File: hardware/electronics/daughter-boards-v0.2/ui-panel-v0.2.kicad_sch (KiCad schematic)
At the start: 9 parts

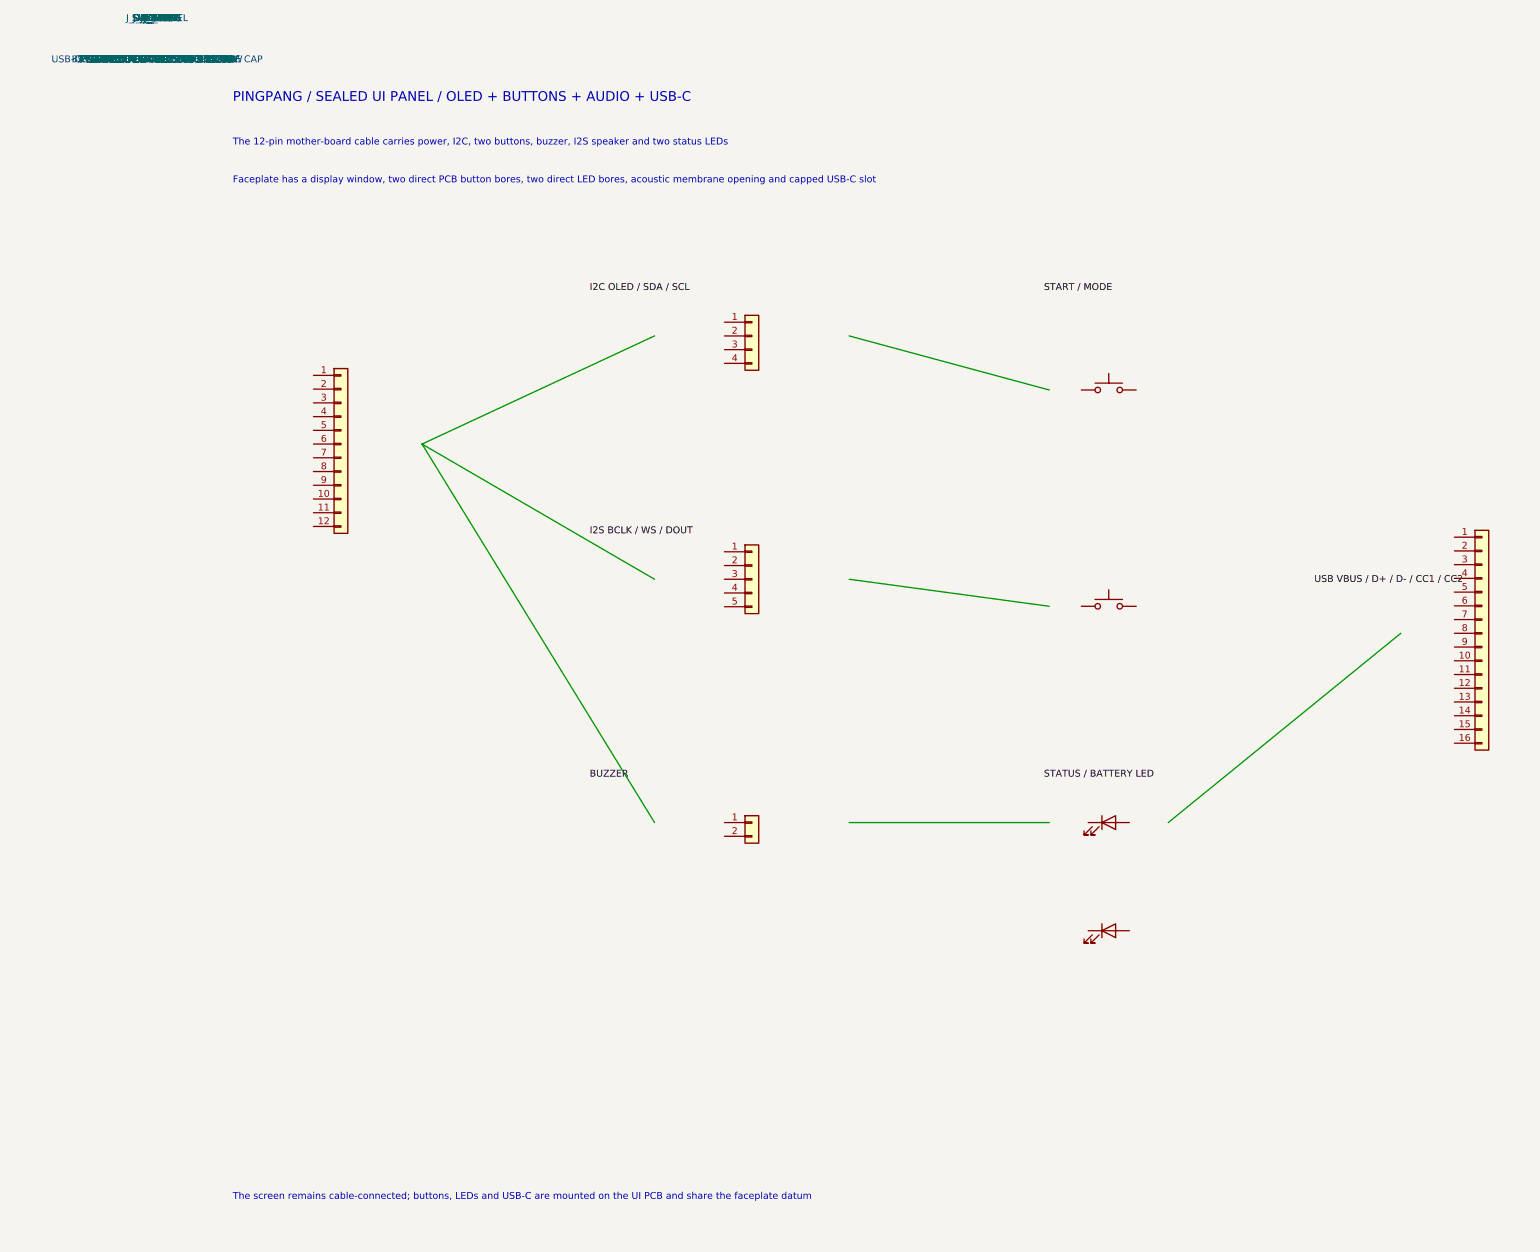
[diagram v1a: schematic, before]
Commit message: 🔌 统一 Type-C 充电入口
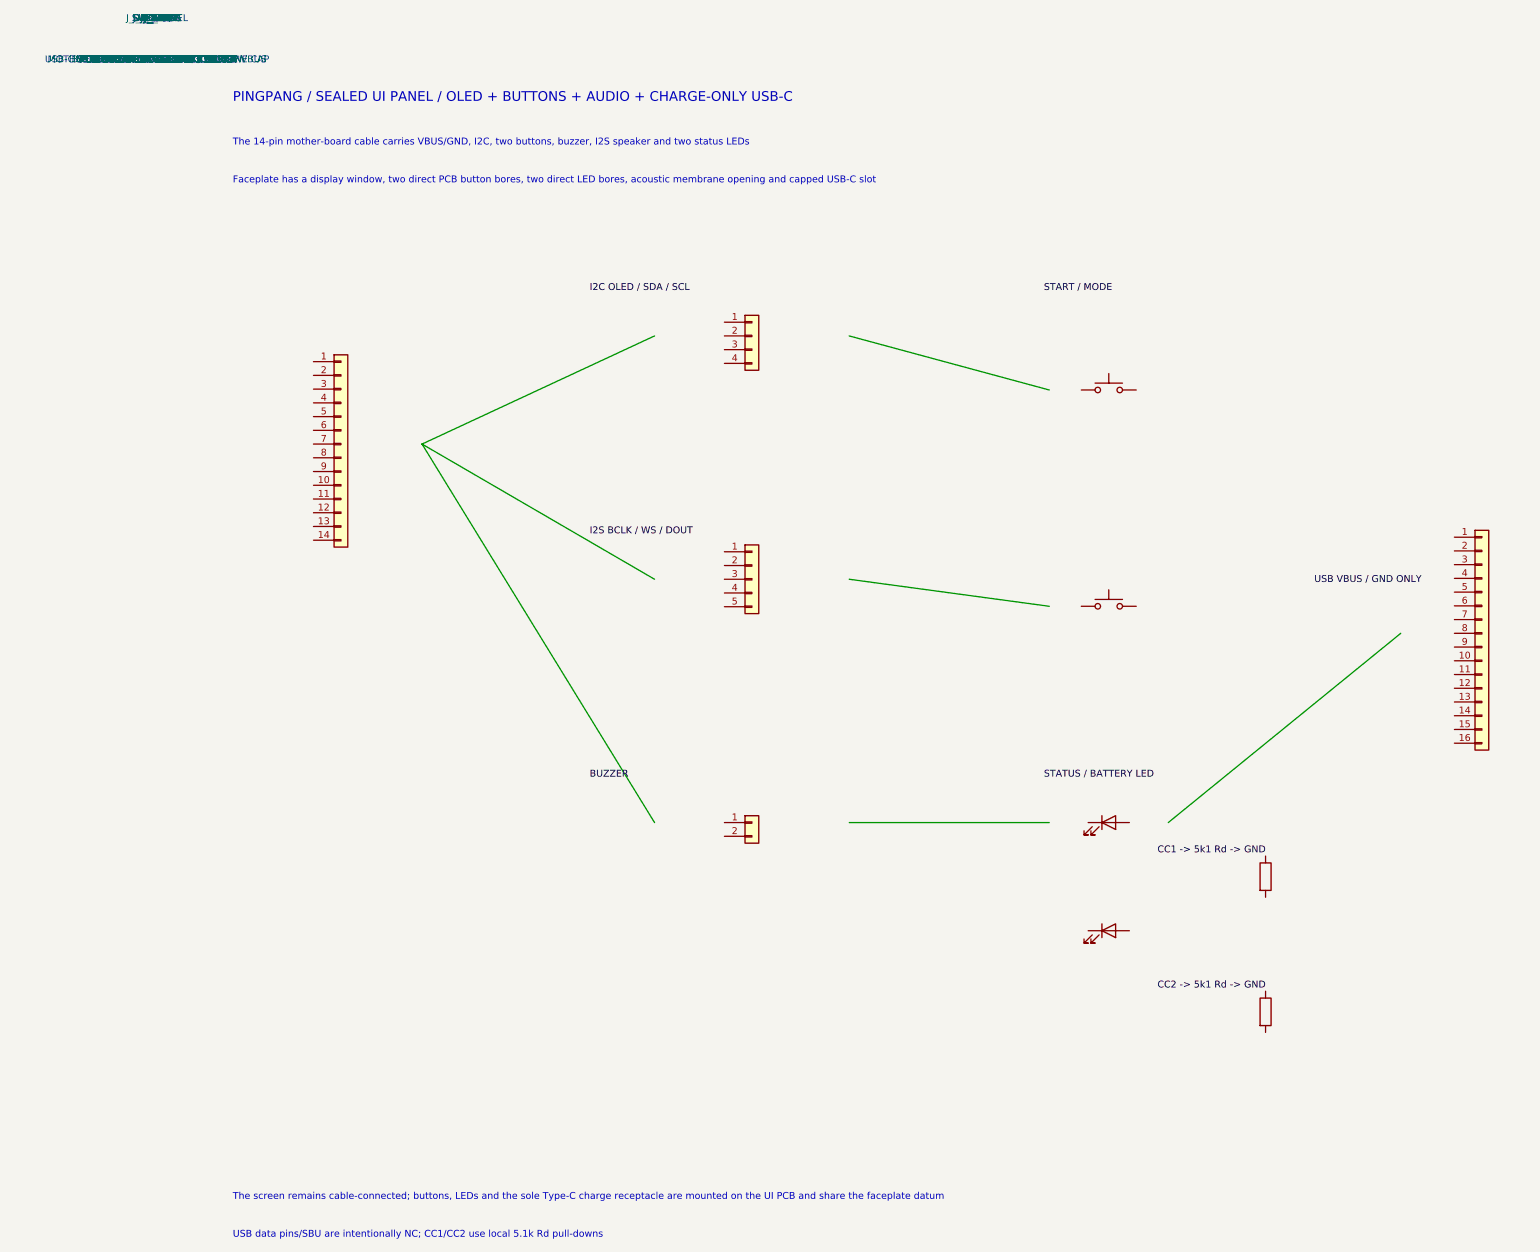
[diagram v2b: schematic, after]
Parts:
- removed J_MOTHER: MOTHER UI MX1.25 LOCK 12P, Connector_JST:JST_GH_SM12B-GHS-TB_1x12-1MP_P1.25mm_Horizontal, symbol Connector_Generic:Conn_01x12
- added J_MOTHER: MOTHER UI MX1.25 LOCK 14P / CHARGE VBUS, Connector_JST:JST_GH_SM14B-GHS-TB_1x14-1MP_P1.25mm_Horizontal, symbol Connector_Generic:Conn_01x14
- added R_CC1: USB-C CC1 Rd 5k1, Resistor_SMD:R_0603_1608Metric, symbol Device:R
- added R_CC2: USB-C CC2 Rd 5k1, Resistor_SMD:R_0603_1608Metric, symbol Device:R
- J_USB_PANEL: value USB-C VERTICAL 16P DIRECT / SILICONE CAP -> USB-C VERTICAL CHARGE-ONLY / SILICONE CAP
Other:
- note added: "PINGPANG / SEALED UI PANEL / OLED + BUTTONS + AUDIO + CHARGE-ONLY USB-C"
- note added: "The 14-pin mother-board cable carries VBUS/GND, I2C, two buttons, buzzer, I2S speaker and two status LEDs"
- note added: "The screen remains cable-connected; buttons, LEDs and the sole Type-C charge receptacle are mounted on the UI PCB and share the faceplate datum"
- note added: "USB data pins/SBU are intentionally NC; CC1/CC2 use local 5.1k Rd pull-downs"
- note removed: "PINGPANG / SEALED UI PANEL / OLED + BUTTONS + AUDIO + USB-C"
- note removed: "The 12-pin mother-board cable carries power, I2C, two buttons, buzzer, I2S speaker and two status LEDs"
- note removed: "The screen remains cable-connected; buttons, LEDs and USB-C are mounted on the UI PCB and share the faceplate datum"
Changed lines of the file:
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@@
 		(comment 3 "Mechanical package is checked separately against net_stand.scad")
 	)
-	(text "PINGPANG / SEALED UI PANEL / OLED + BUTTONS + AUDIO + USB-C"
+	(text "PINGPANG / SEALED UI PANEL / OLED + BUTTONS + AUDIO + CHARGE-ONLY USB-C"
 		(exclude_from_sim no)
 		(at 14 12 0)
 		(effects (font (size 1.8 1.8)) (justify left bottom))
 	)
-	(text "The 12-pin mother-board cable carries power, I2C, two buttons, buzzer, I2S speaker and two status LEDs"
+	(text "The 14-pin mother-board cable carries VBUS/GND, I2C, two buttons, buzzer, I2S speaker and two status LEDs"
 		(exclude_from_sim no)
 		(at 14 20 0)
@@
 		(effects (font (size 1.27 1.27)) (justify left bottom))
 	)
-	(text "The screen remains cable-connected; buttons, LEDs and USB-C are mounted on the UI PCB and share the faceplate datum"
+	(text "The screen remains cable-connected; buttons, LEDs and the sole Type-C charge receptacle are mounted on the UI PCB and share the faceplate datum"
 		(exclude_from_sim no)
 		(at 14 215 0)
+		(effects (font (size 1.27 1.27)) (justify left bottom))
+	)
+	(text "USB data pins/SBU are intentionally NC; CC1/CC2 use local 5.1k Rd pull-downs"
+		(exclude_from_sim no)
+		(at 14 222 0)
 		(effects (font (size 1.27 1.27)) (justify left bottom))
 	)
@@
 		)
 	)
-	(label "USB VBUS / D+ / D- / CC1 / CC2"
+	(label "USB VBUS / GND ONLY"
 		(at 214 101 0)
 		(effects
@@
 		)
 	)
-	(symbol
-		(lib_id "Connector_Generic:Conn_01x12")
+	(label "CC1 -> 5k1 Rd -> GND"
+		(at 185 151 0)
+		(effects
+			(font (size 1.27 1.27))
+			(justify left bottom)
+		)
+	)
+	(label "CC2 -> 5k1 Rd -> GND"
+		(at 185 176 0)
+		(effects
+			(font (size 1.27 1.27))
+			(justify left bottom)
+		)
+	)
+	(symbol
+		(lib_id "Connector_Generic:Conn_01x14")
 		(at 34 75 0)
 		(unit 1)
@@
 			)
 		)
-		(property "Value" "MOTHER UI MX1.25 LOCK 12P"
-			(at 0 3.81 0)
-			(effects
-				(font
-					(size 1.27 1.27)
-				)
-			)
-		)
-		(property "Footprint" "Connector_JST:JST_GH_SM12B-GHS-TB_1x12-1MP_P1.25mm_Horizontal"
+		(property "Value" "MOTHER UI MX1.25 LOCK 14P / CHARGE VBUS"
+			(at 0 3.81 0)
+			(effects
+				(font
+					(size 1.27 1.27)
+				)
+			)
+		)
+		(property "Footprint" "Connector_JST:JST_GH_SM14B-GHS-TB_1x14-1MP_P1.25mm_Horizontal"
 			(at 0 0 0)
 			(effects
@@
 		(pin "12"
 		)
-		(instances
-			(project "ui-panel-v0.2"
-				(path "/f68ee34d-60f0-4cb7-b441-7115130c09d0"
+		(pin "13"
+		)
+		(pin "14"
+		)
+		(instances
+			(project "ui-panel-v0.2"
+				(path "/aeec6c4c-c507-4b2b-bfa8-245ac5a65a05"
 					(reference "J_MOTHER")
 					(unit 1)
@@
 		(instances
 			(project "ui-panel-v0.2"
-				(path "/f68ee34d-60f0-4cb7-b441-7115130c09d0"
+				(path "/aeec6c4c-c507-4b2b-bfa8-245ac5a65a05"
 					(reference "J_OLED")
 					(unit 1)
@@
 		(instances
 			(project "ui-panel-v0.2"
-				(path "/f68ee34d-60f0-4cb7-b441-7115130c09d0"
+				(path "/aeec6c4c-c507-4b2b-bfa8-245ac5a65a05"
 					(reference "J_SPK")
 					(unit 1)
@@
 		(instances
 			(project "ui-panel-v0.2"
-				(path "/f68ee34d-60f0-4cb7-b441-7115130c09d0"
+				(path "/aeec6c4c-c507-4b2b-bfa8-245ac5a65a05"
 					(reference "J_BUZ")
 					(unit 1)
@@
 		(instances
 			(project "ui-panel-v0.2"
-				(path "/f68ee34d-60f0-4cb7-b441-7115130c09d0"
+				(path "/aeec6c4c-c507-4b2b-bfa8-245ac5a65a05"
 					(reference "SW_START")
 					(unit 1)
@@
 		(instances
 			(project "ui-panel-v0.2"
-				(path "/f68ee34d-60f0-4cb7-b441-7115130c09d0"
+				(path "/aeec6c4c-c507-4b2b-bfa8-245ac5a65a05"
 					(reference "SW_MODE")
 					(unit 1)
@@
 		(instances
 			(project "ui-panel-v0.2"
-				(path "/f68ee34d-60f0-4cb7-b441-7115130c09d0"
+				(path "/aeec6c4c-c507-4b2b-bfa8-245ac5a65a05"
 					(reference "D_STATUS")
 					(unit 1)
@@
 		(instances
 			(project "ui-panel-v0.2"
-				(path "/f68ee34d-60f0-4cb7-b441-7115130c09d0"
+				(path "/aeec6c4c-c507-4b2b-bfa8-245ac5a65a05"
 					(reference "D_BAT")
 					(unit 1)
@@
 			)
 		)
-		(property "Value" "USB-C VERTICAL 16P DIRECT / SILICONE CAP"
+		(property "Value" "USB-C VERTICAL CHARGE-ONLY / SILICONE CAP"
 			(at 0 3.81 0)
 			(effects
@@
 		(instances
 			(project "ui-panel-v0.2"
-				(path "/f68ee34d-60f0-4cb7-b441-7115130c09d0"
+				(path "/aeec6c4c-c507-4b2b-bfa8-245ac5a65a05"
 					(reference "J_USB_PANEL")
 					(unit 1)
 				)
+			)
+		)
+	)
+	(symbol
+		(lib_id "Device:R")
+		(at 205 155 0)
+		(unit 1)
+		(exclude_from_sim no)
+		(in_bom yes)
+		(on_board yes)
+		(dnp no)
+		(property "Reference" "R_CC1"
+			(at 0 -3.81 0)
+			(effects
+				(font
+					(size 1.27 1.27)
+				)
+			)
+		)
+		(property "Value" "USB-C CC1 Rd 5k1"
+			(at 0 3.81 0)
+			(effects
+				(font
+					(size 1.27 1.27)
+				)
+			)
+		)
+		(property "Footprint" "Resistor_SMD:R_0603_1608Metric"
+			(at 0 0 0)
+			(effects
+				(font
+					(size 1.27 1.27)
+				)
+				(hide yes)
+			)
+		)
+		(property "Datasheet" "~"
+			(at 0 0 0)
+			(effects
+				(font
+					(size 1.27 1.27)
+				)
+				(hide yes)
+			)
+		)
+		(property "Description" "Pingpang SmartGear connectorized control path"
+			(at 0 0 0)
+			(effects
+				(font
+					(size 1.27 1.27)
+				)
+				(hide yes)
+			)
+		)
+		(pin "1"
+		)
+		(pin "2"
+		)
+		(instances
+			(project "ui-panel-v0.2"
+				(path "/aeec6c4c-c507-4b2b-bfa8-245ac5a65a05"
+					(reference "R_CC1")
+					(unit 1)
+				)
+			)
+		)
+	)
+	(symbol
+		(lib_id "Device:R")
+		(at 205 180 0)
+		(unit 1)
+		(exclude_from_sim no)
+		(in_bom yes)
+		(on_board yes)
+		(dnp no)
+		(property "Reference" "R_CC2"
+			(at 0 -3.81 0)
+			(effects
+				(font
+					(size 1.27 1.27)
+				)
+			)
+		)
+		(property "Value" "USB-C CC2 Rd 5k1"
+			(at 0 3.81 0)
+			(effects
+				(font
+					(size 1.27 1.27)
+				)
+			)
+		)
+		(property "Footprint" "Resistor_SMD:R_0603_1608Metric"
+			(at 0 0 0)
+			(effects
+				(font
+					(size 1.27 1.27)
+				)
+				(hide yes)
+			)
+		)
+		(property "Datasheet" "~"
+			(at 0 0 0)
+			(effects
+				(font
+					(size 1.27 1.27)
+				)
+				(hide yes)
+			)
+		)
+		(property "Description" "Pingpang SmartGear connectorized control path"
+			(at 0 0 0)
+			(effects
+				(font
+					(size 1.27 1.27)
+				)
+				(hide yes)
+			)
+		)
+		(pin "1"
+		)
+		(pin "2"
+		)
+		(instances
+			(project "ui-panel-v0.2"
+				(path "/aeec6c4c-c507-4b2b-bfa8-245ac5a65a05"
+					(reference "R_CC2")
+					(unit 1)
+				)

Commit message: 🔌 修复线束契约与电子机械干涉
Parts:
- J_USB_PANEL: footprint Connector_USB:USB_C_Receptacle_G-Switch_GT-USB-7051x -> Connector_USB:USB_C_Receptacle_GCT_USB4105-xx-A_16P_TopMnt_Horizontal
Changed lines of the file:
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@@
 		(instances
 			(project "ui-panel-v0.2"
-				(path "/aeec6c4c-c507-4b2b-bfa8-245ac5a65a05"
+				(path "/77da9e6c-d3ab-4e4b-9de0-5313cfb908bb"
 					(reference "J_MOTHER")
 					(unit 1)
@@
 		(instances
 			(project "ui-panel-v0.2"
-				(path "/aeec6c4c-c507-4b2b-bfa8-245ac5a65a05"
+				(path "/77da9e6c-d3ab-4e4b-9de0-5313cfb908bb"
 					(reference "J_OLED")
 					(unit 1)
@@
 		(instances
 			(project "ui-panel-v0.2"
-				(path "/aeec6c4c-c507-4b2b-bfa8-245ac5a65a05"
+				(path "/77da9e6c-d3ab-4e4b-9de0-5313cfb908bb"
 					(reference "J_SPK")
 					(unit 1)
@@
 		(instances
 			(project "ui-panel-v0.2"
-				(path "/aeec6c4c-c507-4b2b-bfa8-245ac5a65a05"
+				(path "/77da9e6c-d3ab-4e4b-9de0-5313cfb908bb"
 					(reference "J_BUZ")
 					(unit 1)
@@
 		(instances
 			(project "ui-panel-v0.2"
-				(path "/aeec6c4c-c507-4b2b-bfa8-245ac5a65a05"
+				(path "/77da9e6c-d3ab-4e4b-9de0-5313cfb908bb"
 					(reference "SW_START")
 					(unit 1)
@@
 		(instances
 			(project "ui-panel-v0.2"
-				(path "/aeec6c4c-c507-4b2b-bfa8-245ac5a65a05"
+				(path "/77da9e6c-d3ab-4e4b-9de0-5313cfb908bb"
 					(reference "SW_MODE")
 					(unit 1)
@@
 		(instances
 			(project "ui-panel-v0.2"
-				(path "/aeec6c4c-c507-4b2b-bfa8-245ac5a65a05"
+				(path "/77da9e6c-d3ab-4e4b-9de0-5313cfb908bb"
 					(reference "D_STATUS")
 					(unit 1)
@@
 		(instances
 			(project "ui-panel-v0.2"
-				(path "/aeec6c4c-c507-4b2b-bfa8-245ac5a65a05"
+				(path "/77da9e6c-d3ab-4e4b-9de0-5313cfb908bb"
 					(reference "D_BAT")
 					(unit 1)
@@
 			)
 		)
-		(property "Footprint" "Connector_USB:USB_C_Receptacle_G-Switch_GT-USB-7051x"
+		(property "Footprint" "Connector_USB:USB_C_Receptacle_GCT_USB4105-xx-A_16P_TopMnt_Horizontal"
 			(at 0 0 0)
 			(effects
@@
 		(instances
 			(project "ui-panel-v0.2"
-				(path "/aeec6c4c-c507-4b2b-bfa8-245ac5a65a05"
+				(path "/77da9e6c-d3ab-4e4b-9de0-5313cfb908bb"
 					(reference "J_USB_PANEL")
 					(unit 1)
@@
 		(instances
 			(project "ui-panel-v0.2"
-				(path "/aeec6c4c-c507-4b2b-bfa8-245ac5a65a05"
+				(path "/77da9e6c-d3ab-4e4b-9de0-5313cfb908bb"
 					(reference "R_CC1")
 					(unit 1)
@@
 		(instances
 			(project "ui-panel-v0.2"
-				(path "/aeec6c4c-c507-4b2b-bfa8-245ac5a65a05"
+				(path "/77da9e6c-d3ab-4e4b-9de0-5313cfb908bb"
 					(reference "R_CC2")
 					(unit 1)
